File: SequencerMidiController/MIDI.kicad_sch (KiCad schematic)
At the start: 11 parts, among them J1 MDIN-5, J2 MIDI OUT, U42 74LVC1G34, U43 6N135S

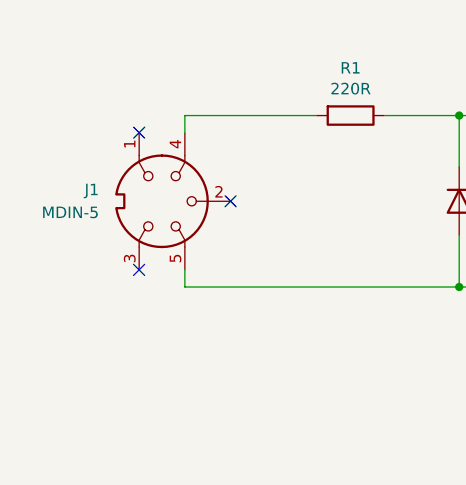
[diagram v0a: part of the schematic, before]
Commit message: updated layout DRC
Fixed clearance errors with polygons and pads in switch footprints
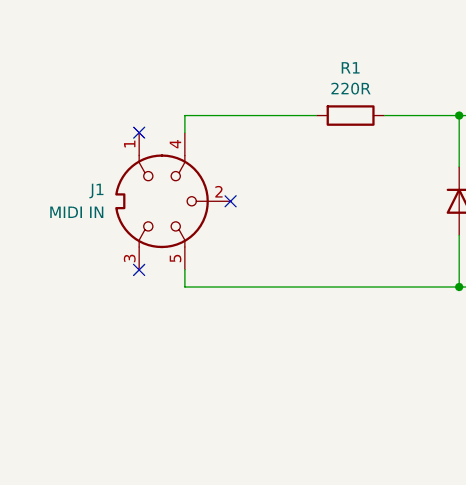
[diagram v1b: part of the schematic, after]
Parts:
- J1: value MDIN-5 -> MIDI IN
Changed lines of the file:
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@@
   (symbol (lib_id "MidiDin5:DIN-5") (at 83.82 47.625 270) (unit 1)
     (in_bom yes) (on_board yes) (fields_autoplaced)
-    (property "Reference" "J1" (id 0) (at 76.835 46.3599 90)
+    (property "Reference" "J1" (id 0) (at 77.47 46.355 90)
       (effects (font (size 1.27 1.27)) (justify right))
     )
-    (property "Value" "MDIN-5" (id 1) (at 76.835 48.8999 90)
+    (property "Value" "MIDI IN" (id 1) (at 77.47 48.895 90)
       (effects (font (size 1.27 1.27)) (justify right))
     )

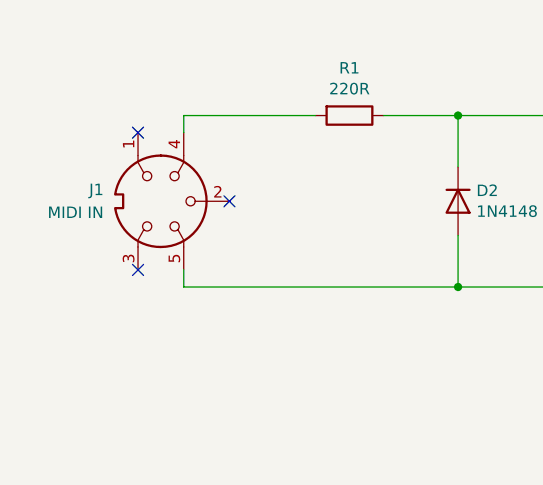
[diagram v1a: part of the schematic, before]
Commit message: Checked microSD card connector pins and added board layout connector footprint
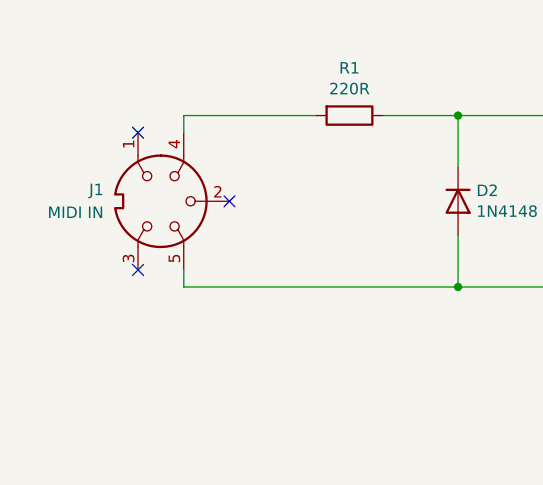
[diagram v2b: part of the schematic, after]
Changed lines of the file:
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@@
     (pin "1")
   )
-  (symbol (lib_id "MidiDin5:DIN-5") (at 83.82 47.625 270) (unit 1)
+  (symbol (lib_name "DIN-5_1") (lib_id "MidiDin5:DIN-5") (at 83.82 47.625 270) (unit 1)
     (in_bom yes) (on_board yes) (fields_autoplaced)
     (property "Reference" "J1" (id 0) (at 77.47 46.355 90)

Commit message: RevB
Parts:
- J1: value MIDI IN -> MIDI_IN
- J2: value MIDI OUT -> MIDI_OUT
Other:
- moved on the sheet: R1
